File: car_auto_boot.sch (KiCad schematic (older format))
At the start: 15 parts, among them J1A1 Power_Terminal_1, J1B1 Power_Terminal_2, J2 Signal_Terminal, J3 Conn_01x05, SW2 SW_1, U1 ProMicro, U2 HW399_bo, U3 GY712_bo

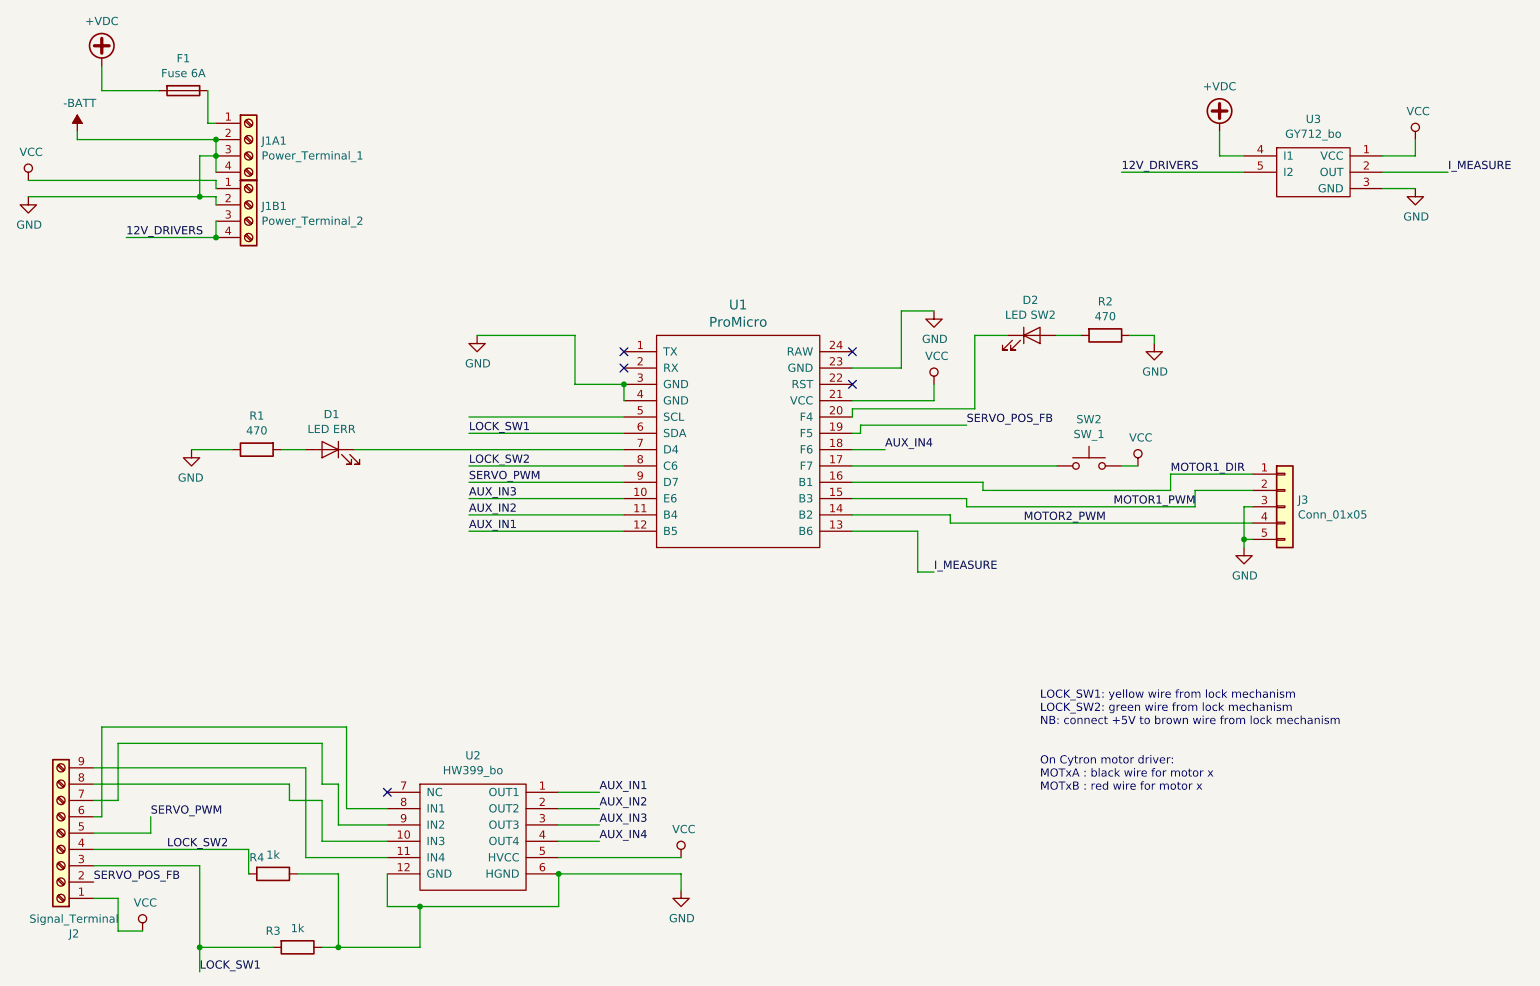
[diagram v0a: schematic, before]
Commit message: version with mosfet
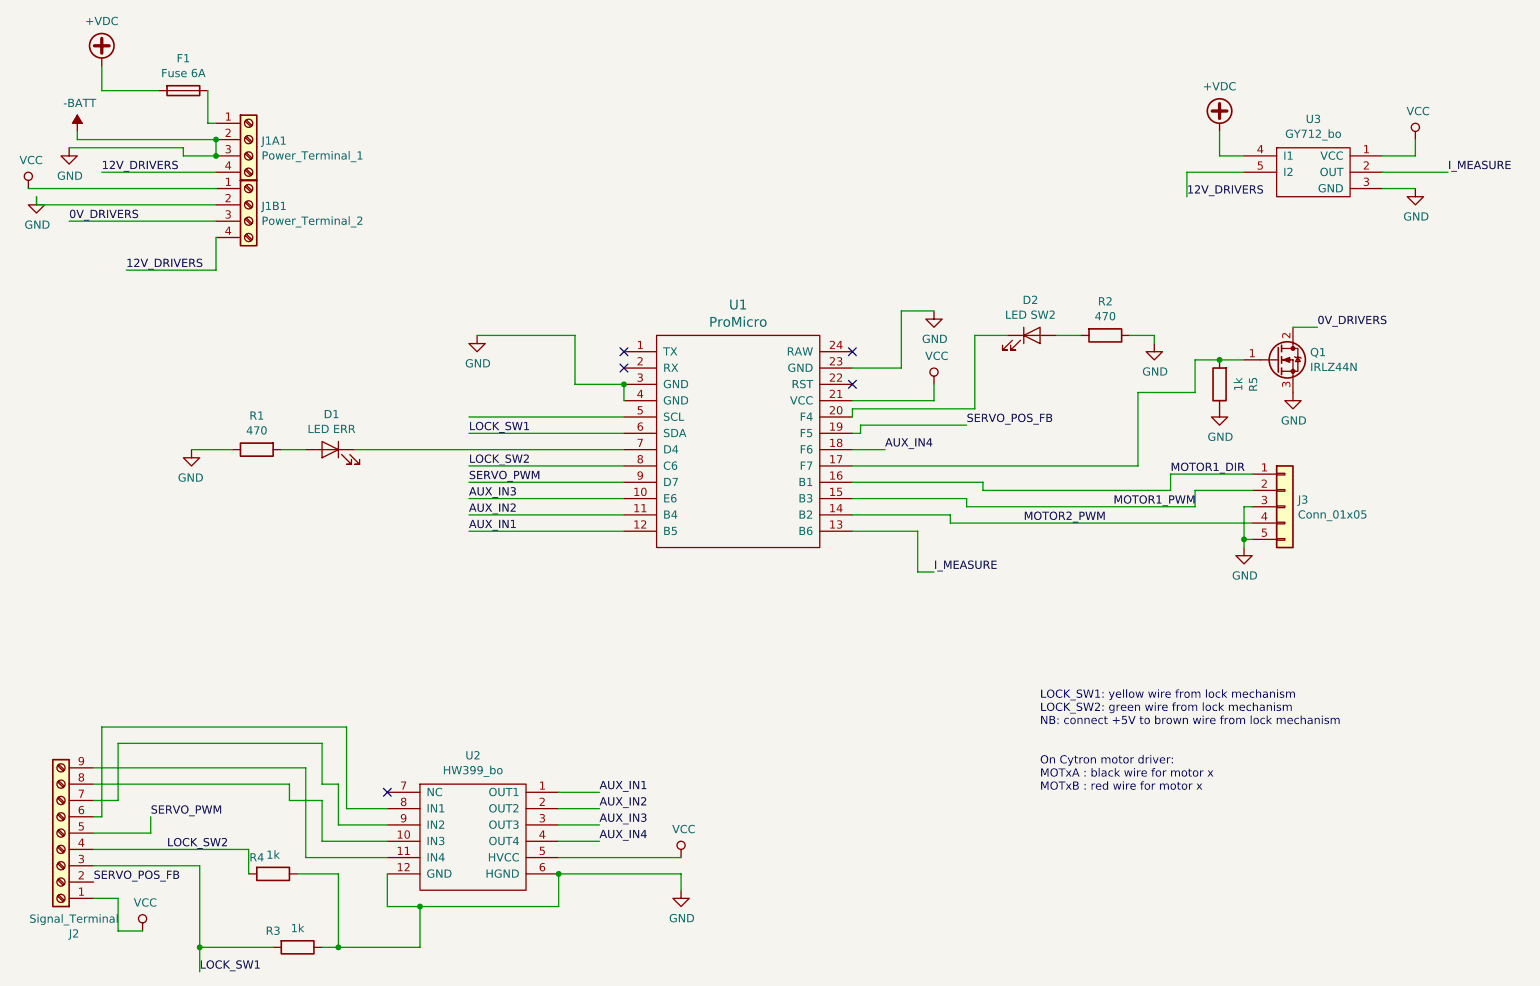
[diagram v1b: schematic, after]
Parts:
- removed SW2: SW_1, Buttons_Switches_THT:SW_TH_Tactile_Omron_B3F-10xx, symbol Switch:SW_Push
- added Q1: IRLZ44N, TO_SOT_Packages_THT:TO-220-3_Vertical, symbol Transistor_FET:IRLZ44N
- added R5: 1k, Resistors_THT:R_Axial_DIN0207_L6.3mm_D2.5mm_P7.62mm_Horizontal, symbol Device:R
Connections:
- net -BATT: now also Q1.3 (S), R5.1; no longer J1A1.4 (Pin_4)
- net 12V_DRIVERS: now also J1A1.4 (Pin_4); no longer J1B1.3 (Pin_3)
- net at U1.17 (F7): now also Q1.1 (G), R5.2
- new net 0V_DRIVERS: J1B1.3 (Pin_3), Q1.2 (D)
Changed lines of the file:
@@
 L power:GND #PWR0103
 U 1 1 5C23E573
-P 1450 1900
-F 0 "#PWR0103" H 1450 1650 50  0001 C CNN
-F 1 "GND" H 1455 1727 50  0000 C CNN
-F 2 "" H 1450 1900 50  0001 C CNN
-F 3 "" H 1450 1900 50  0001 C CNN
-	1    1450 1900
+P 1500 1900
+F 0 "#PWR0103" H 1500 1650 50  0001 C CNN
+F 1 "GND" H 1505 1727 50  0000 C CNN
+F 2 "" H 1500 1900 50  0001 C CNN
+F 3 "" H 1500 1900 50  0001 C CNN
+	1    1500 1900
 	1    0    0    -1
 $EndComp
@@
 L power:VCC #PWR0105
 U 1 1 5C23E769
-P 1450 1800
-F 0 "#PWR0105" H 1450 1650 50  0001 C CNN
-F 1 "VCC" H 1467 1973 50  0000 C CNN
-F 2 "" H 1450 1800 50  0001 C CNN
-F 3 "" H 1450 1800 50  0001 C CNN
-	1    1450 1800
+P 1450 1850
+F 0 "#PWR0105" H 1450 1700 50  0001 C CNN
+F 1 "VCC" H 1467 2023 50  0000 C CNN
+F 2 "" H 1450 1850 50  0001 C CNN
+F 3 "" H 1450 1850 50  0001 C CNN
+	1    1450 1850
 	1    0    0    -1
 $EndComp
@@
 	1750 1550 1750 1500
 Wire Wire Line
-	1450 1800 2600 1800
-Wire Wire Line
-	2600 1800 2600 1850
-Wire Wire Line
-	2600 1900 2600 1950
-Wire Wire Line
-	2600 2050 2600 2150
-Text Label 2050 2150 0    50   ~ 0
+	1450 1850 2600 1850
+Text Label 2050 2350 0    50   ~ 0
 12V_DRIVERS
-Wire Wire Line
-	2600 2150 2050 2150
 Wire Wire Line
 	9750 1850 9950 1850
@@
 Wire Wire Line
 	8750 1650 8750 1500
-Text Label 8150 1750 0    50   ~ 0
+Text Label 8550 1900 0    50   ~ 0
 12V_DRIVERS
 Wire Wire Line
-	8900 1750 8150 1750
+	8900 1750 8550 1750
 $Comp
 L Device:Fuse F1
@@
 Wire Wire Line
 	3850 6250 3650 6250
-$Comp
-L Switch:SW_Push SW2
-U 1 1 5C2BF90F
-P 7950 3550
-F 0 "SW2" H 7950 3835 50  0000 C CNN
-F 1 "SW_1" H 7950 3744 50  0000 C CNN
-F 2 "Buttons_Switches_THT:SW_TH_Tactile_Omron_B3F-10xx" H 7950 3750 50  0001 C CNN
-F 3 "" H 7950 3750 50  0001 C CNN
-	1    7950 3550
-	1    0    0    -1
-$EndComp
-$Comp
-L power:VCC #PWR0115
-U 1 1 5C2BF985
-P 8250 3550
-F 0 "#PWR0115" H 8250 3400 50  0001 C CNN
-F 1 "VCC" H 8267 3723 50  0000 C CNN
-F 2 "" H 8250 3550 50  0001 C CNN
-F 3 "" H 8250 3550 50  0001 C CNN
-	1    8250 3550
-	1    0    0    -1
-$EndComp
 Text Label 7550 3900 0    50   ~ 0
 MOTOR2_PWM
@@
 	1    0    0    -1
 $EndComp
-Wire Wire Line
-	2600 1650 2600 1750
 $Comp
 L Connector:Screw_Terminal_01x04 J1B1
@@
 	1    0    0    -1
 $EndComp
-Connection ~ 2600 2150
 Wire Wire Line
 	2600 1550 2600 1650
 Connection ~ 2600 1550
 Connection ~ 2600 1650
-Wire Wire Line
-	2500 1900 2500 1650
-Wire Wire Line
-	2500 1650 2600 1650
-Wire Wire Line
-	1450 1900 2500 1900
-Connection ~ 2500 1900
-Wire Wire Line
-	2500 1900 2600 1900
 $Comp
 L power:GND #PWR0117
@@
 Wire Wire Line
 	6550 3350 6500 3350
-Wire Wire Line
-	8150 3550 8250 3550
-Wire Wire Line
-	6500 3550 7750 3550
 Text Label 4150 3650 0    50   ~ 0
 SERVO_PWM
@@
 Text Notes 7650 5550 0    50   ~ 0
 LOCK_SW1: yellow wire from lock mechanism\nLOCK_SW2: green wire from lock mechanism\nNB: connect +5V to brown wire from lock mechanism\n\n\nOn Cytron motor driver:\nMOTxA : black wire for motor x\nMOTxB : red wire for motor x
+$Comp
+L Transistor_FET:IRLZ44N Q1
+U 1 1 5C320BD9
+P 9100 2900
+F 0 "Q1" H 9305 2946 50  0000 L CNN
+F 1 "IRLZ44N" H 9305 2855 50  0000 L CNN
+F 2 "TO_SOT_Packages_THT:TO-220-3_Vertical" H 9350 2825 50  0001 L CIN
+F 3 "http://www.irf.com/product-info/datasheets/data/irlz44n.pdf" H 9100 2900 50  0001 L CNN
+	1    9100 2900
+	1    0    0    -1
+$EndComp
+Wire Wire Line
+	8550 1900 8550 1750
+Wire Wire Line
+	9200 2700 9350 2700
+Text Label 9350 2700 0    50   ~ 0
+0V_DRIVERS
+$Comp
+L Device:R R5
+U 1 1 5C3315EE
+P 8750 3050
+F 0 "R5" V 8543 3050 50  0000 C CNN
+F 1 "1k" V 8634 3050 50  0000 C CNN
+F 2 "Resistors_THT:R_Axial_DIN0207_L6.3mm_D2.5mm_P7.62mm_Horizontal" V 8680 3050 50  0001 C CNN
+F 3 "~" H 8750 3050 50  0001 C CNN
+	1    8750 3050
+	-1   0    0    1
+$EndComp
+$Comp
+L power:GND #PWR01
+U 1 1 5C331696
+P 9200 3100
+F 0 "#PWR01" H 9200 2850 50  0001 C CNN
+F 1 "GND" H 9205 2927 50  0000 C CNN
+F 2 "" H 9200 3100 50  0001 C CNN
+F 3 "" H 9200 3100 50  0001 C CNN
+	1    9200 3100
+	1    0    0    -1
+$EndComp
+Wire Wire Line
+	6500 3550 8250 3550
+Wire Wire Line
+	2400 1600 2400 1650
+Wire Wire Line
+	2400 1650 2600 1650
+Text Label 1700 2050 0    50   ~ 0
+0V_DRIVERS
+Wire Wire Line
+	2600 1950 1500 1950
+Wire Wire Line
+	1500 1950 1500 1900
+Wire Wire Line
+	2600 2050 1700 2050
+Wire Wire Line
+	2600 2150 2600 2350
+Wire Wire Line
+	2600 2350 2050 2350
+Text Label 1900 1750 0    50   ~ 0
+12V_DRIVERS
+Wire Wire Line
+	2600 1750 1900 1750
+$Comp
+L power:GND #PWR?
+U 1 1 5C37C722
+P 1700 1600
+F 0 "#PWR?" H 1700 1350 50  0001 C CNN
+F 1 "GND" H 1705 1427 50  0000 C CNN
+F 2 "" H 1700 1600 50  0001 C CNN
+F 3 "" H 1700 1600 50  0001 C CNN
+	1    1700 1600
+	1    0    0    -1
+$EndComp
+Wire Wire Line
+	1700 1600 2400 1600
+Wire Wire Line
+	8750 2900 8900 2900
+$Comp
+L power:GND #PWR?
+U 1 1 5C390484
+P 8750 3200
+F 0 "#PWR?" H 8750 2950 50  0001 C CNN
+F 1 "GND" H 8755 3027 50  0000 C CNN
+F 2 "" H 8750 3200 50  0001 C CNN
+F 3 "" H 8750 3200 50  0001 C CNN
+	1    8750 3200
+	1    0    0    -1
+$EndComp
+Wire Wire Line
+	8250 3550 8250 3100
+Wire Wire Line
+	8250 3100 8600 3100
+Wire Wire Line
+	8600 3100 8600 2900
+Wire Wire Line
+	8600 2900 8750 2900
+Connection ~ 8750 2900
 $EndSCHEMATC
